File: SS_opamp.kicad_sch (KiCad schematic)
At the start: 79 parts

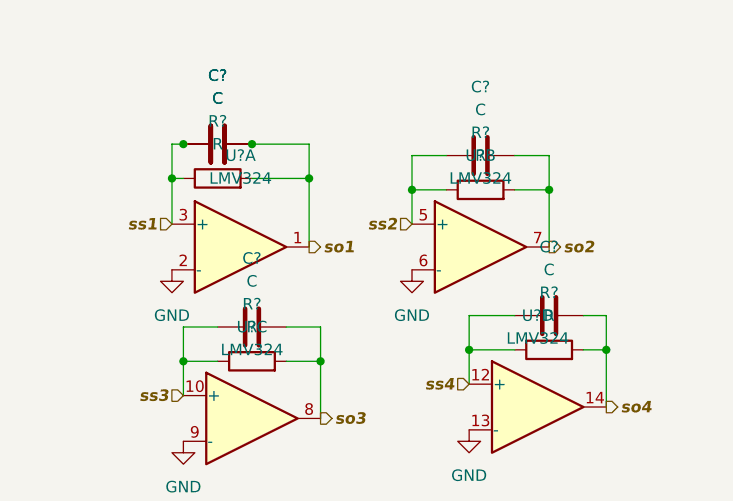
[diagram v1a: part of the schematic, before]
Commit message: sun sensor connector connected
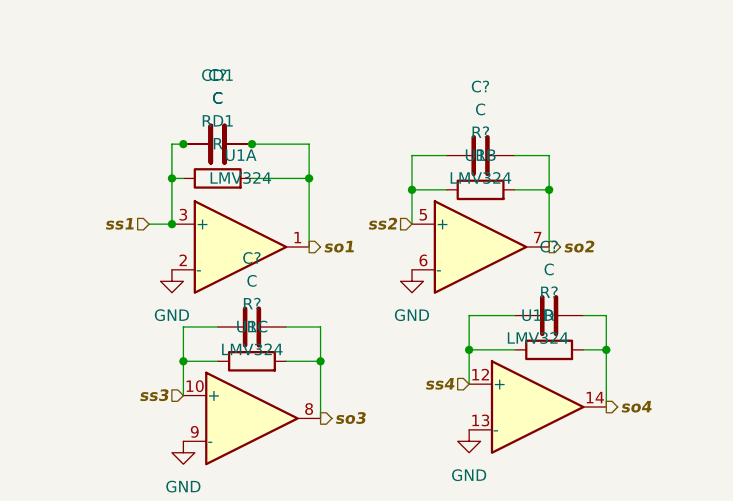
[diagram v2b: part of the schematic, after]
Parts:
- gave numbers to parts that had none: 3
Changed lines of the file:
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@@
 (kicad_sch (version 20211123) (generator eeschema)
   (paper "A4")
+  (junction (at 30.48 33.02) (diameter 0) (color 0 0 0 0)
+  )
   (junction (at 102.87 189.23) (diameter 0) (color 0 0 0 0)
   )
@@
   )
   (wire (pts (xy 151.13 82.55) (xy 151.13 86.36))
+    (stroke (width 0) (type default) (color 0 0 0 0))
+  )
+  (wire (pts (xy 27.94 33.02) (xy 30.48 33.02))
     (stroke (width 0) (type default) (color 0 0 0 0))
   )
@@
     (effects (font (size 1.27 1.27) bold italic) (justify right))
   )
-  (hierarchical_label "ss1" (shape input) (at 30.48 33.02 180)
+  (hierarchical_label "ss1" (shape input) (at 27.94 33.02 180)
     (effects (font (size 1.27 1.27) bold italic) (justify right))
   )
@@
   (symbol (lib_id "Amplifier_Operational:LMV324") (at 71.12 53.34 0) (unit 4)
     (in_bom yes) (on_board yes) (fields_autoplaced)
-    (property "Reference" "U?" (id 0) (at 71.12 43.18 0))
+    (property "Reference" "U1" (id 0) (at 71.12 43.18 0))
     (property "Value" "LMV324" (id 1) (at 71.12 45.72 0))
     (property "Footprint" "" (id 2) (at 69.85 50.8 0)
@@
   (symbol (lib_id "Amplifier_Operational:LMV324") (at 39.37 54.61 0) (unit 3)
     (in_bom yes) (on_board yes) (fields_autoplaced)
-    (property "Reference" "U?" (id 0) (at 39.37 44.45 0))
+    (property "Reference" "U1" (id 0) (at 39.37 44.45 0))
     (property "Value" "LMV324" (id 1) (at 39.37 46.99 0))
     (property "Footprint" "" (id 2) (at 38.1 52.07 0)
@@
   (symbol (lib_id "Device:C") (at 35.56 24.13 90) (unit 1)
     (in_bom yes) (on_board yes) (fields_autoplaced)
-    (property "Reference" "C?" (id 0) (at 35.56 16.51 90))
+    (property "Reference" "CD1" (id 0) (at 35.56 16.51 90))
     (property "Value" "C" (id 1) (at 35.56 19.05 90))
     (property "Footprint" "" (id 2) (at 39.37 23.1648 0)
@@
   (symbol (lib_id "Amplifier_Operational:LMV324") (at 64.77 35.56 0) (unit 2)
     (in_bom yes) (on_board yes) (fields_autoplaced)
-    (property "Reference" "U?" (id 0) (at 64.77 25.4 0))
+    (property "Reference" "U1" (id 0) (at 64.77 25.4 0))
     (property "Value" "LMV324" (id 1) (at 64.77 27.94 0))
     (property "Footprint" "" (id 2) (at 63.5 33.02 0)
@@
   (symbol (lib_id "Amplifier_Operational:LMV324") (at 38.1 35.56 0) (unit 1)
     (in_bom yes) (on_board yes) (fields_autoplaced)
-    (property "Reference" "U?" (id 0) (at 38.1 25.4 0))
+    (property "Reference" "U1" (id 0) (at 38.1 25.4 0))
     (property "Value" "LMV324" (id 1) (at 38.1 27.94 0))
     (property "Footprint" "" (id 2) (at 36.83 33.02 0)
@@
   (symbol (lib_id "Device:R") (at 35.56 27.94 90) (unit 1)
     (in_bom yes) (on_board yes) (fields_autoplaced)
-    (property "Reference" "R?" (id 0) (at 35.56 21.59 90))
+    (property "Reference" "RD1" (id 0) (at 35.56 21.59 90))
     (property "Value" "R" (id 1) (at 35.56 24.13 90))
     (property "Footprint" "" (id 2) (at 35.56 29.718 90)

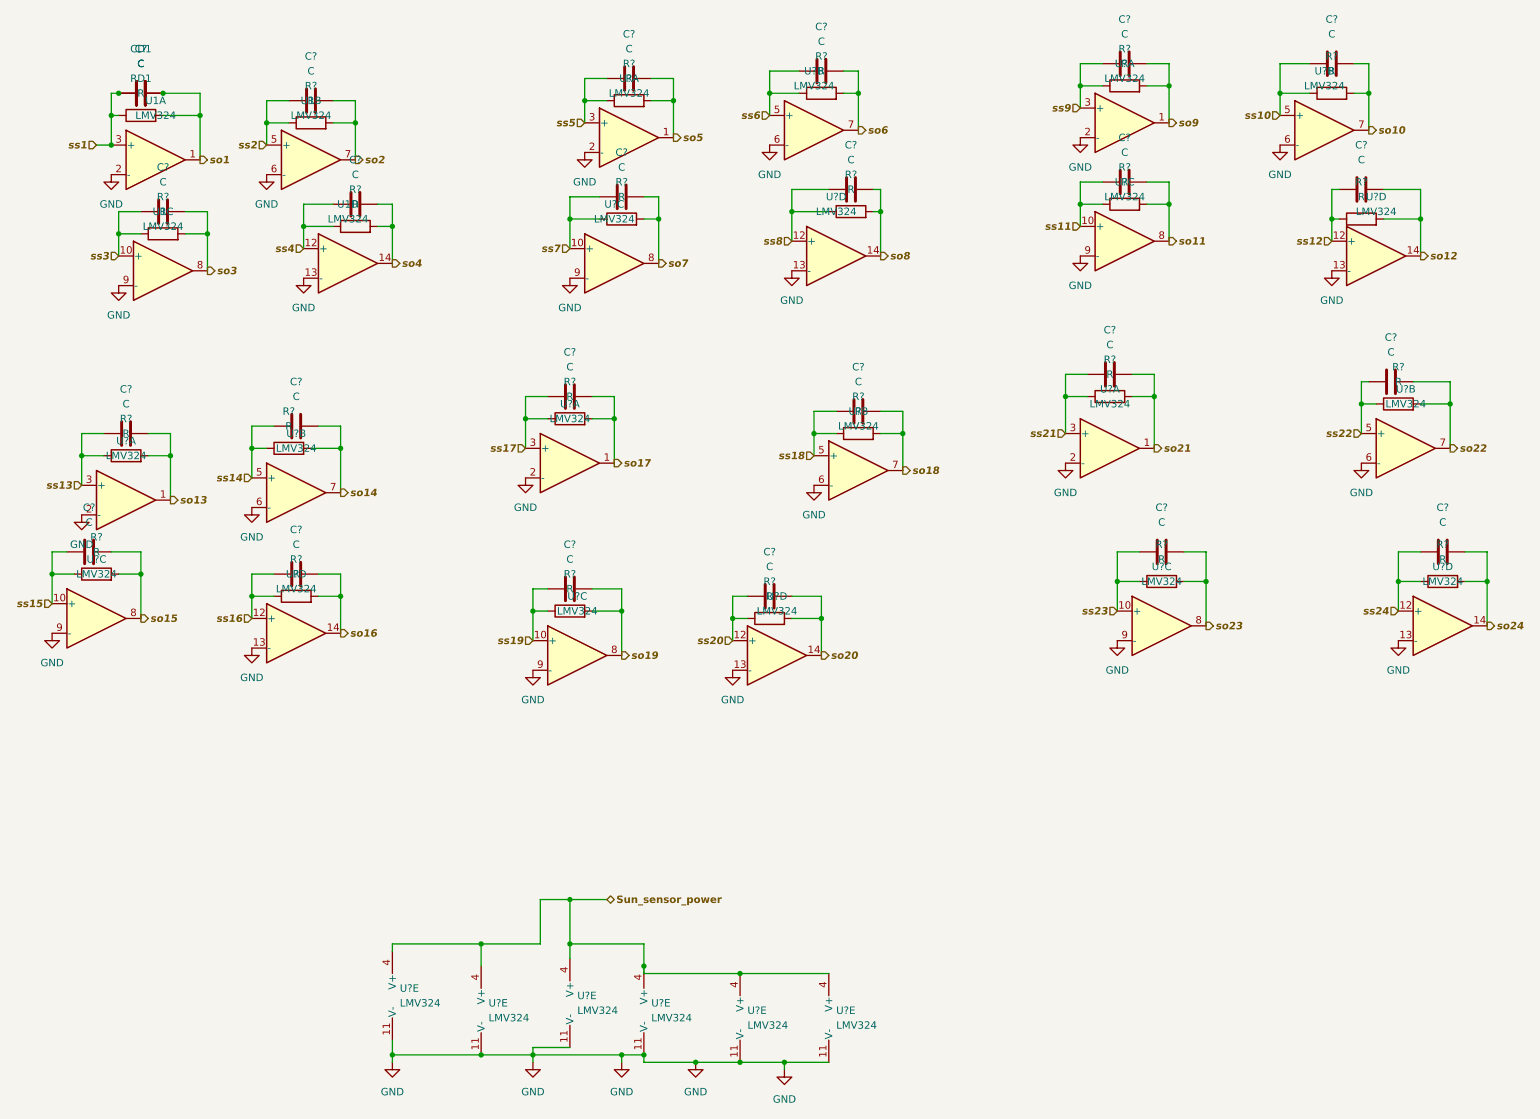
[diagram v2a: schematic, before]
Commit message: Sun-sensor circuit reorganised
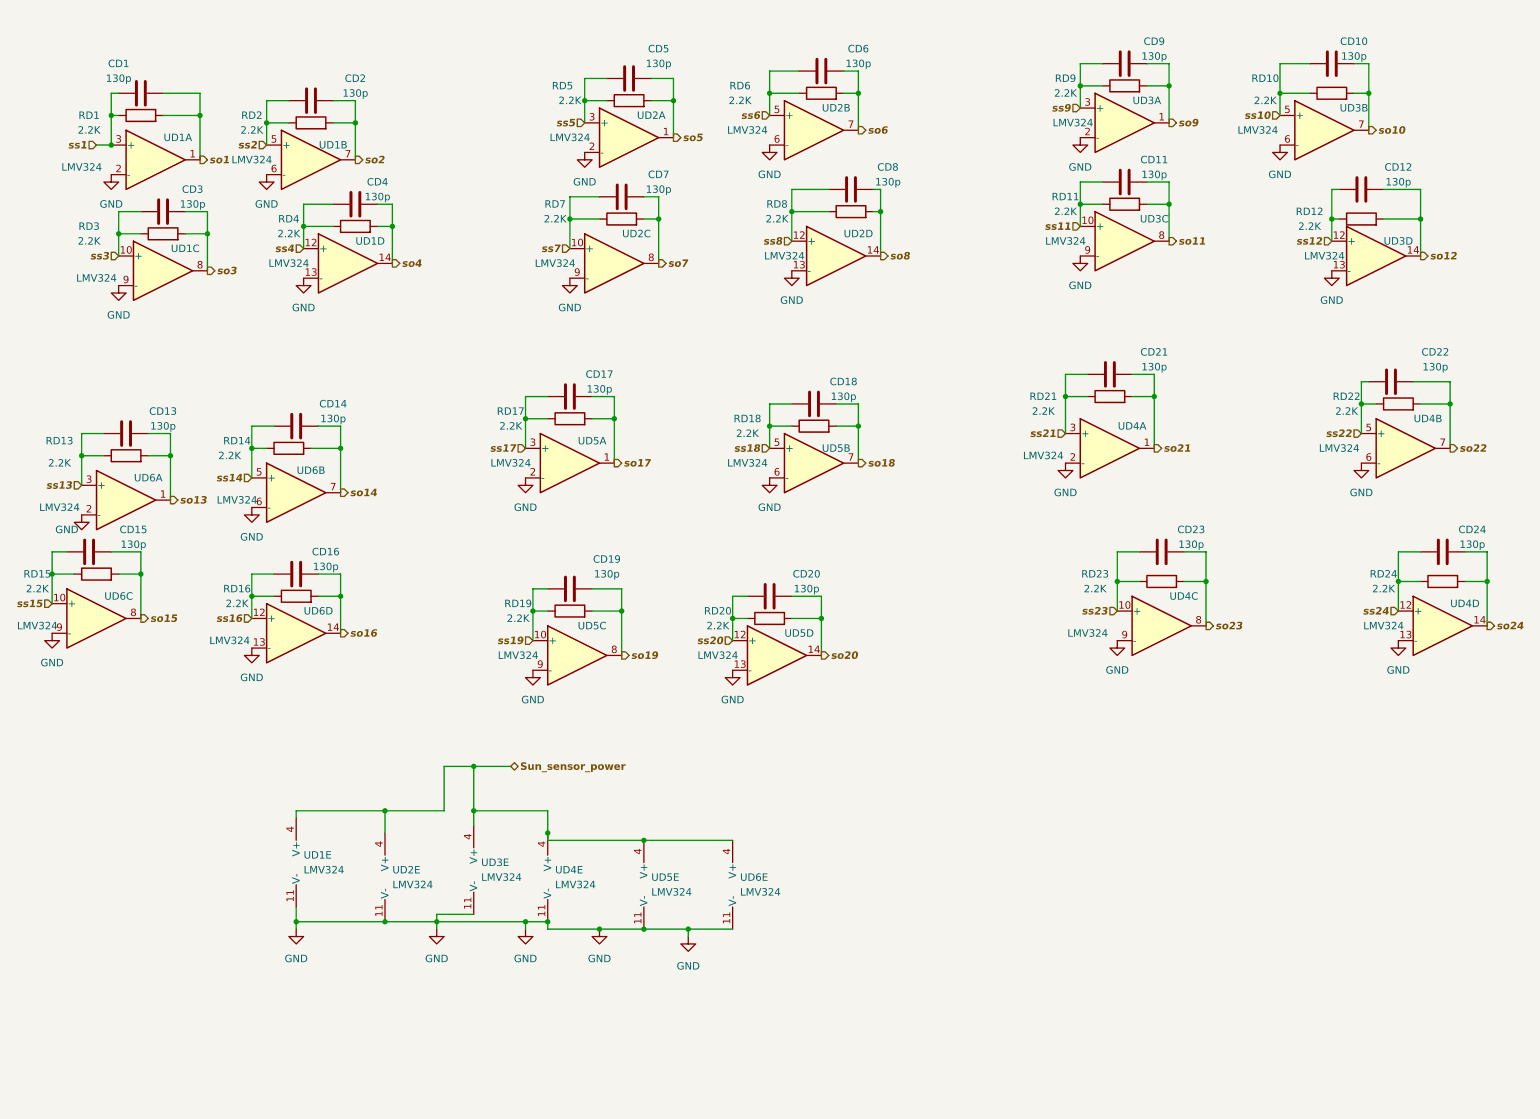
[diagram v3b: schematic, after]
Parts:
- removed C?: C, symbol Device:C
- CD1: value C -> 130p
- CD10, CD11, CD12, CD13, CD14, CD15, CD16, CD17, CD18, CD19, CD2, CD20, CD21, CD22, CD23, CD24, CD3, CD4, CD5, CD6, CD7, CD8, CD9: renamed from C?; value C -> 130p
- RD1: value R -> 2.2K
- RD10, RD11, RD12, RD13, RD14, RD15, RD16, RD17, RD18, RD19, RD2, RD20, RD21, RD22, RD23, RD24, RD3, RD4, RD5, RD6, RD7, RD8, RD9: renamed from R?; value R -> 2.2K
- gave numbers to parts that had none: 6
- renumbered U1 to UD1
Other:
- moved on the sheet: CD18, RD18, UD1E, UD2E, UD3E, UD4E, UD5B, UD5E, UD6E

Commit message: MCU interfaces are done! Check the Changes and Complete ERC modifications
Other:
- company: (none) -> Parikshit Student Satellite Team
- title: (none) -> AOCS BOARD
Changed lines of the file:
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@@
 (kicad_sch (version 20211123) (generator eeschema)
   (paper "A4")
+  (title_block
+    (title "AOCS BOARD")
+    (company "Parikshit Student Satellite Team")
+  )
   (junction (at 30.48 33.02) (diameter 0) (color 0 0 0 0)
   )
@@
   )
   (wire (pts (xy 109.22 45.72) (xy 109.22 50.8))
+    (stroke (width 0) (type default) (color 0 0 0 0))
+  )
+  (wire (pts (xy 29.845 174.625) (xy 29.845 173.355))
     (stroke (width 0) (type default) (color 0 0 0 0))
   )
@@
     (pin "4")
   )
+  (symbol (lib_id "power:PWR_FLAG") (at 29.845 173.355 0) (unit 1)
+    (in_bom yes) (on_board yes) (fields_autoplaced)
+    (property "Reference" "#FLG0105" (id 0) (at 29.845 171.45 0)
+      (effects (font (size 1.27 1.27)) hide)
+    )
+    (property "Value" "PWR_FLAG" (id 1) (at 29.845 167.64 0))
+    (property "Footprint" "" (id 2) (at 29.845 173.355 0)
+      (effects (font (size 1.27 1.27)) hide)
+    )
+    (property "Datasheet" "~" (id 3) (at 29.845 173.355 0)
+      (effects (font (size 1.27 1.27)) hide)
+    )
+    (pin "1")
+  )
   (symbol (lib_id "Device:C") (at 250.19 73.66 90) (unit 1)
     (in_bom yes) (on_board yes)
@@
       (effects (font (size 1.27 1.27)) hide)
     )
+    (pin "1")
+  )
+  (symbol (lib_id "power:GND") (at 29.845 174.625 0) (unit 1)
+    (in_bom yes) (on_board yes) (fields_autoplaced)
+    (property "Reference" "#PWR0269" (id 0) (at 29.845 180.975 0)
+      (effects (font (size 1.27 1.27)) hide)
+    )
+    (property "Value" "GND" (id 1) (at 29.845 179.07 0))
+    (property "Footprint" "" (id 2) (at 29.845 174.625 0)
+      (effects (font (size 1.27 1.27)) hide)
+    )
+    (property "Datasheet" "" (id 3) (at 29.845 174.625 0)
+      (effects (font (size 1.27 1.27)) hide)
+    )

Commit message: Updated the changes
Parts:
- renumbered CD9 to CD1, CD7 to CD10, CD4 to CD11, CD3 to CD12, CD21 to CD13, CD22 to CD14, CD17 to CD15, CD18 to CD16, CD14 to CD17, CD13 to CD18, CD15 to CD19, CD10 to CD2, CD23 to CD20, CD24 to CD21, CD16 to CD22, CD19 to CD23, CD20 to CD24, CD6 to CD3, CD5 to CD4, CD1 to CD5, CD2 to CD6, CD11 to CD7, CD12 to CD9, RD9 to RD1, RD12 to RD10, RD4 to RD11, RD3 to RD12, RD21 to RD13, RD22 to RD14, RD17 to RD15, RD18 to RD16, RD14 to RD17, RD13 to RD18, RD15 to RD19, RD6 to RD2, RD23 to RD20, RD24 to RD21, RD16 to RD22, RD19 to RD23, RD20 to RD24, RD10 to RD3, RD5 to RD4, RD1 to RD5, RD2 to RD6, RD11 to RD7, RD7 to RD9, UD3 to UD1, UD1 to UD3

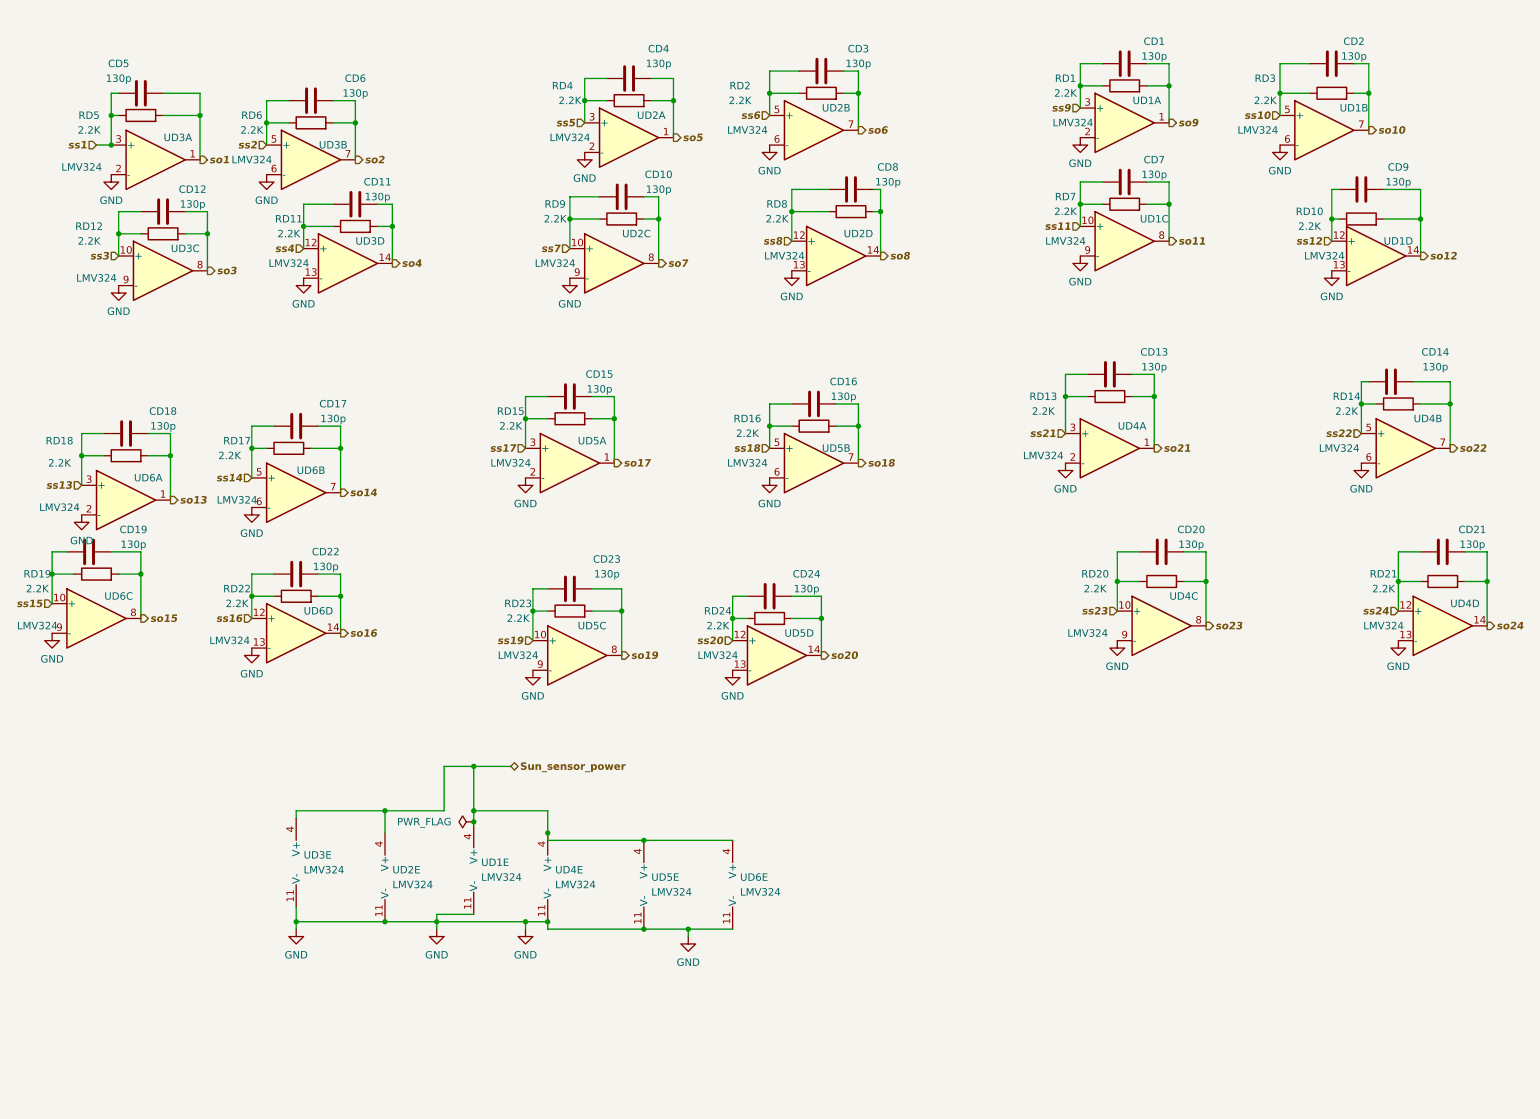
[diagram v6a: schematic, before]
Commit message: Page settings changed. Added some testpoints. Some comments are made.
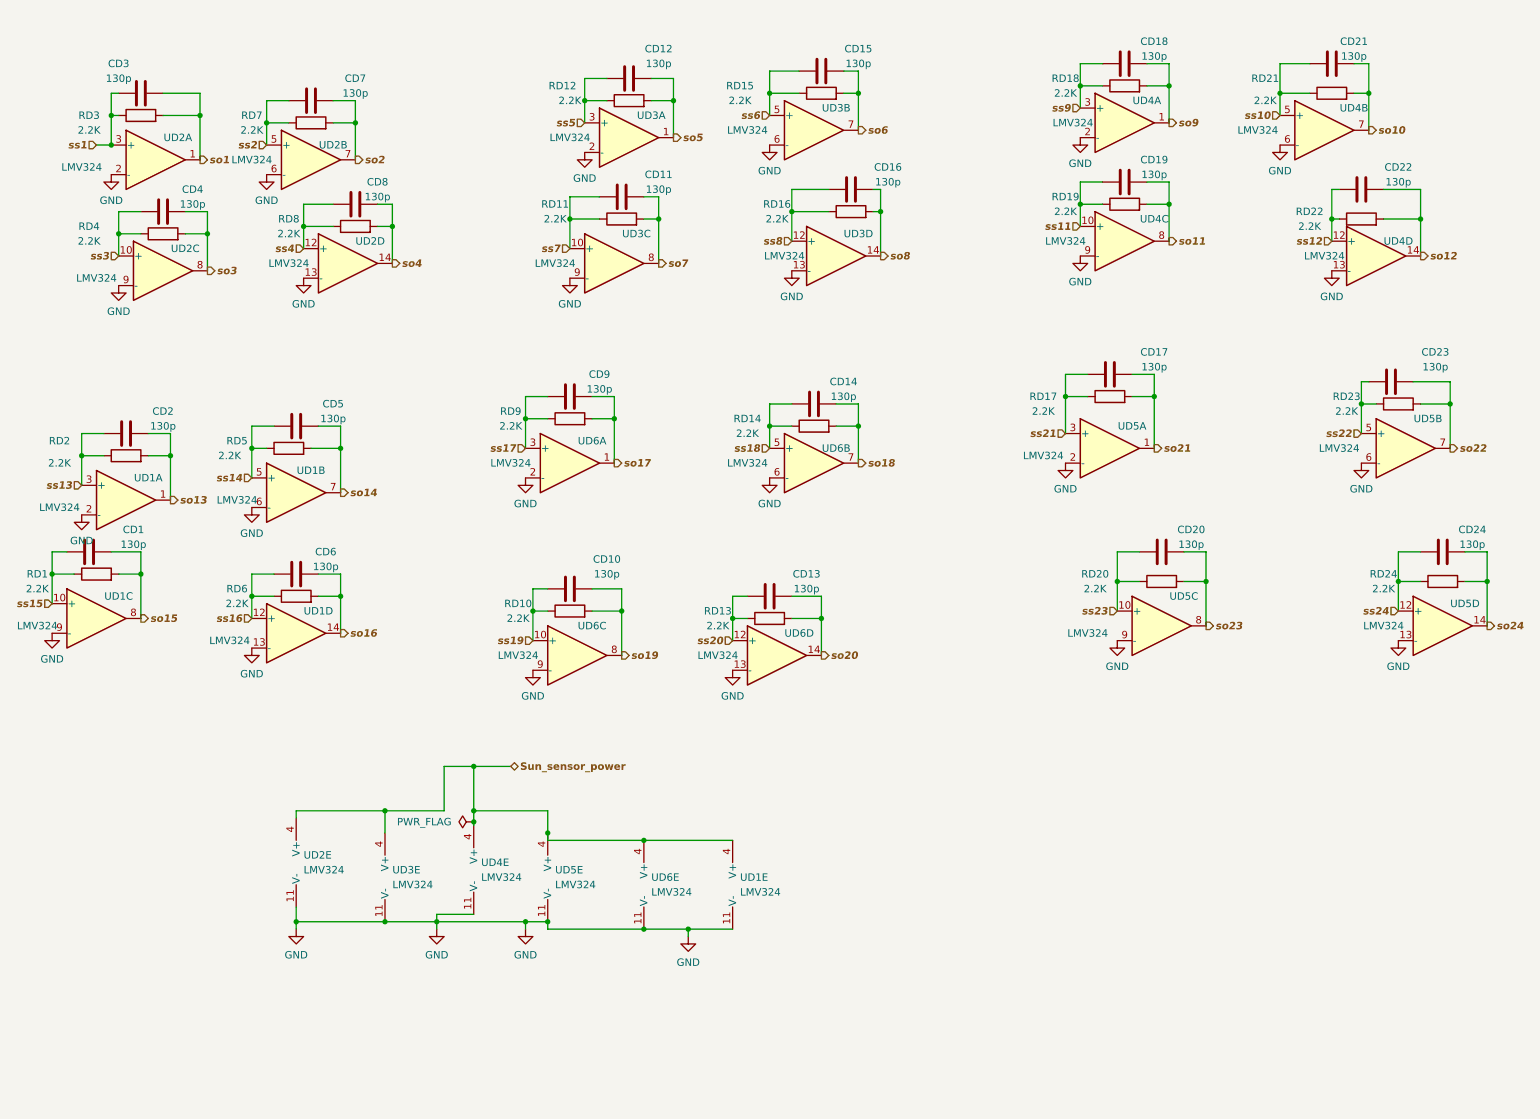
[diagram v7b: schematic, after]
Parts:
- renumbered CD19 to CD1, CD23 to CD10, CD10 to CD11, CD4 to CD12, CD24 to CD13, CD16 to CD14, CD3 to CD15, CD8 to CD16, CD13 to CD17, CD1 to CD18, CD7 to CD19, CD18 to CD2, CD2 to CD21, CD9 to CD22, CD14 to CD23, CD21 to CD24, CD5 to CD3, CD12 to CD4, CD17 to CD5, CD22 to CD6, CD6 to CD7, CD11 to CD8, CD15 to CD9, RD19 to RD1, RD23 to RD10, RD9 to RD11, RD4 to RD12, RD24 to RD13, RD16 to RD14, RD2 to RD15, RD8 to RD16, RD13 to RD17, RD1 to RD18, RD7 to RD19, RD18 to RD2, RD3 to RD21, RD10 to RD22, RD14 to RD23, RD21 to RD24, RD5 to RD3, RD12 to RD4, RD17 to RD5, RD22 to RD6, RD6 to RD7, RD11 to RD8, RD15 to RD9, UD6 to UD1, UD3 to UD2, UD2 to UD3, UD1 to UD4, UD4 to UD5, UD5 to UD6

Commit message: I2C lines are pulled up
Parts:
- CD1, CD10, CD11, CD12, CD13, CD14, CD15, CD16, CD17, CD18, CD19, CD2, CD20, CD21, CD22, CD23, CD24, CD3, CD4, CD5, CD6, CD7, CD8, CD9: footprint (none) -> Capacitor_SMD:C_0603_1608Metric
- RD1, RD10, RD11, RD12, RD13, RD14, RD15, RD16, RD17, RD18, RD19, RD2, RD20, RD21, RD22, RD23, RD24, RD3, RD4, RD5, RD6, RD7, RD8, RD9: footprint (none) -> Resistor_SMD:R_0603_1608Metric
